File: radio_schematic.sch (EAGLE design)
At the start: 29 parts, among them J1 AUDIO_JACK_3.5MM_KIT, J2 AUDIO_JACK_3.5MM_KIT

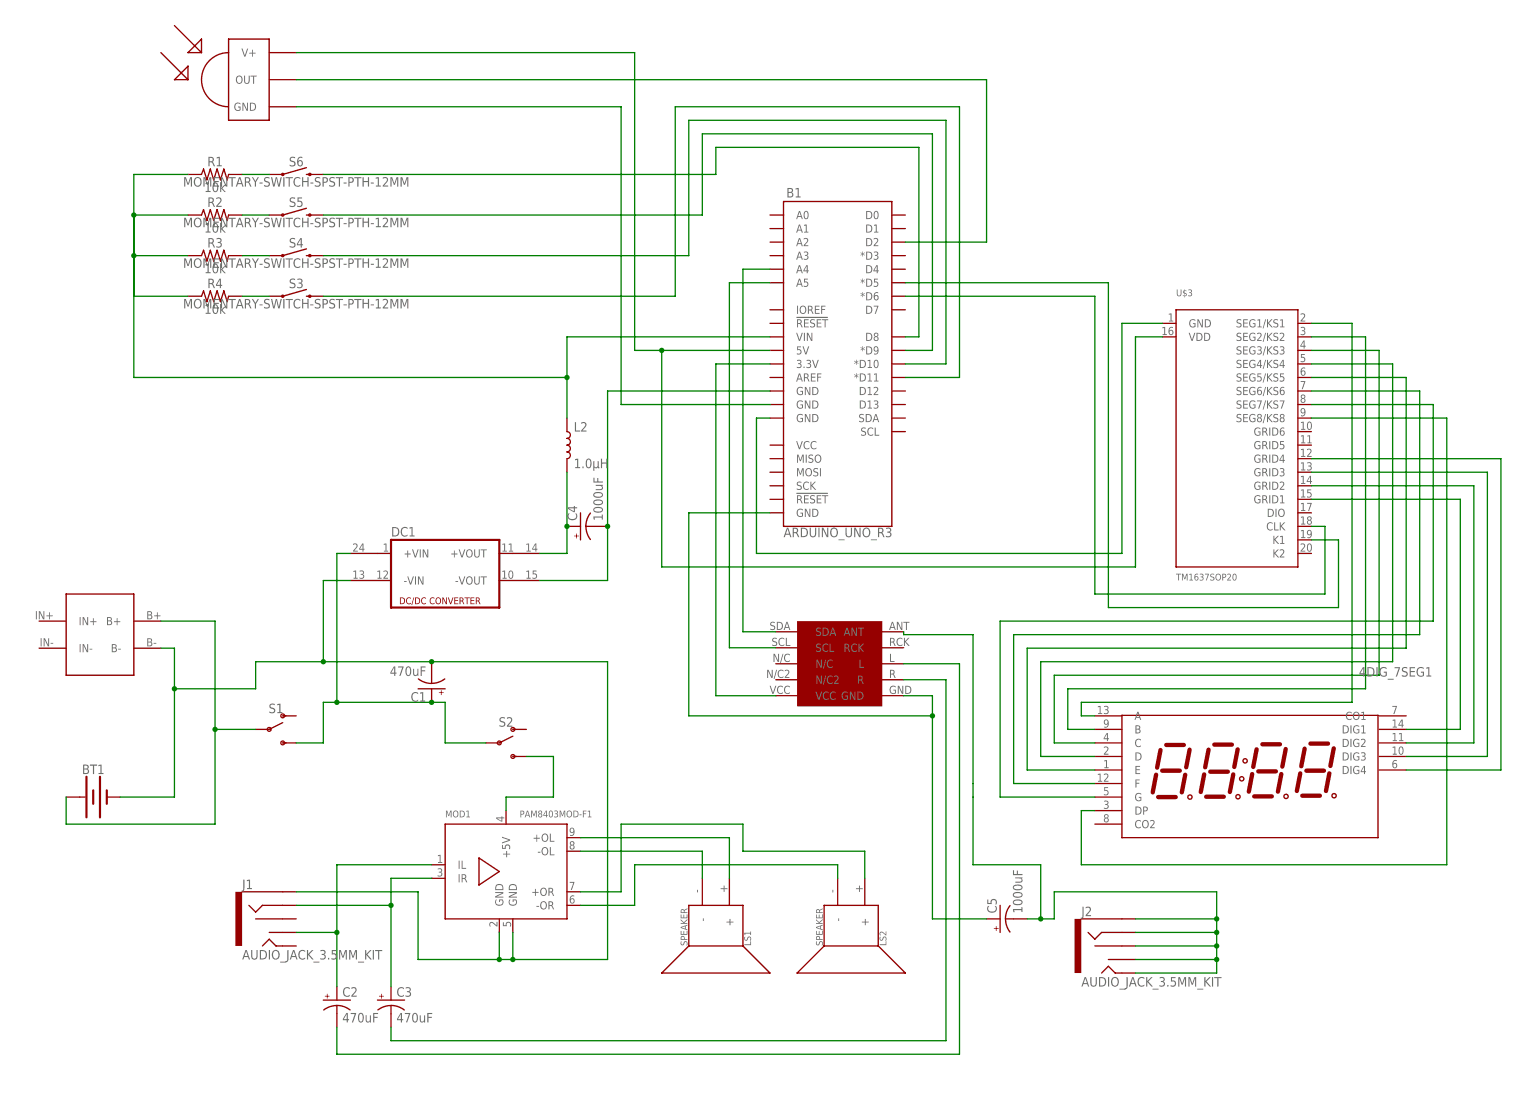
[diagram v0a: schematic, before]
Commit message: sch: add descriptions to all components and divide per section
Signed-off-by: Flopster101 <nahuelgomez329@gmail.com>
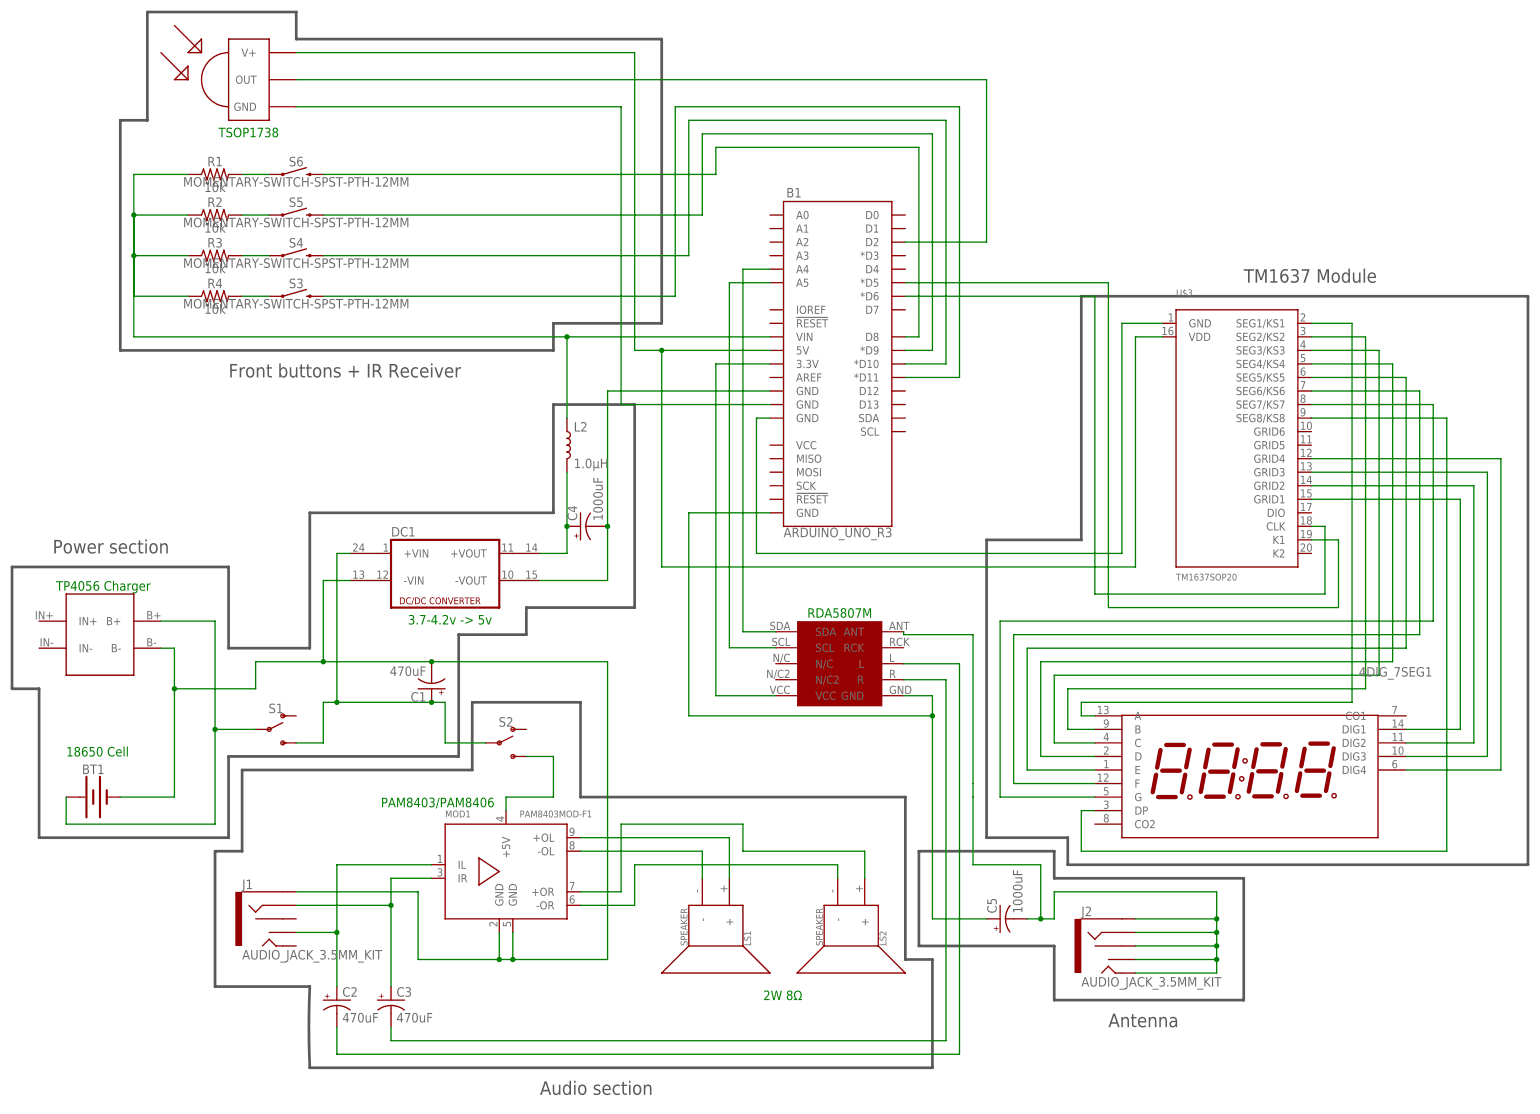
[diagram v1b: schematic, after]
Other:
- note added: "18650 Cell"
- note added: "2W 8Ω"
- note added: "3.7-4.2v -> 5v"
- note added: "Antenna"
- note added: "Audio section"
- note added: "Front buttons + IR Receiver"
- note added: "PAM8403/PAM8406"
- note added: "Power section"
- note added: "RDA5807M"
- note added: "TM1637 Module"
- note added: "TP4056 Charger"
- note added: "TSOP1738"
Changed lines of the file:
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@@
 <setting verticaltext="up"/>
 </settings>
-<grid distance="0.1" unitdist="inch" unit="inch" style="lines" multiple="1" display="no" altdistance="0.01" altunitdist="inch" altunit="inch"/>
+<grid distance="0.1" unitdist="inch" unit="inch" style="lines" multiple="1" display="yes" altdistance="0.01" altunitdist="inch" altunit="inch"/>
 <layers>
 <layer number="1" name="Top" color="4" fill="1" visible="no" active="no"/>
@@
 <sheet>
 <plain>
+<text x="98.425" y="109.855" size="1.778" layer="91">RDA5807M</text>
+<text x="23.495" y="108.585" size="1.778" layer="91">3.7-4.2v -&gt; 5v</text>
+<text x="-42.545" y="114.935" size="1.778" layer="91">TP4056 Charger</text>
+<text x="-40.64" y="83.82" size="1.778" layer="91">18650 Cell</text>
+<text x="18.415" y="74.295" size="1.778" layer="91">PAM8403/PAM8406</text>
+<text x="90.17" y="38.1" size="1.778" layer="91">2W 8Ω</text>
+<text x="-12.065" y="200.025" size="1.778" layer="91">TSOP1738</text>
+<wire x1="147.32" y1="63.5" x2="233.68" y2="63.5" width="0.508" layer="97"/>
+<wire x1="233.68" y1="63.5" x2="233.68" y2="170.18" width="0.508" layer="97"/>
+<wire x1="233.68" y1="170.18" x2="149.86" y2="170.18" width="0.508" layer="97"/>
+<wire x1="149.86" y1="170.18" x2="149.86" y2="124.46" width="0.508" layer="97"/>
+<wire x1="149.86" y1="124.46" x2="132.08" y2="124.46" width="0.508" layer="97"/>
+<wire x1="132.08" y1="124.46" x2="132.08" y2="68.58" width="0.508" layer="97"/>
+<wire x1="132.08" y1="68.58" x2="147.32" y2="68.58" width="0.508" layer="97"/>
+<wire x1="147.32" y1="68.58" x2="147.32" y2="63.5" width="0.508" layer="97"/>
+<text x="180.34" y="172.72" size="2.54" layer="97">TM1637 Module</text>
+<wire x1="144.78" y1="38.1" x2="180.34" y2="38.1" width="0.508" layer="97"/>
+<wire x1="180.34" y1="38.1" x2="180.34" y2="60.96" width="0.508" layer="97"/>
+<wire x1="180.34" y1="60.96" x2="144.78" y2="60.96" width="0.508" layer="97"/>
+<wire x1="144.78" y1="60.96" x2="144.78" y2="66.04" width="0.508" layer="97"/>
+<wire x1="144.78" y1="66.04" x2="119.38" y2="66.04" width="0.508" layer="97"/>
+<wire x1="119.38" y1="66.04" x2="119.38" y2="48.26" width="0.508" layer="97"/>
+<wire x1="119.38" y1="48.26" x2="144.78" y2="48.26" width="0.508" layer="97"/>
+<wire x1="144.78" y1="48.26" x2="144.78" y2="38.1" width="0.508" layer="97"/>
+<text x="154.94" y="33.02" size="2.54" layer="97">Antenna</text>
+<wire x1="35.56" y1="93.98" x2="35.56" y2="81.28" width="0.508" layer="97"/>
+<wire x1="35.56" y1="81.28" x2="-7.62" y2="81.28" width="0.508" layer="97"/>
+<wire x1="-7.62" y1="81.28" x2="-7.62" y2="66.04" width="0.508" layer="97"/>
+<wire x1="-7.62" y1="66.04" x2="-12.7" y2="66.04" width="0.508" layer="97"/>
+<wire x1="-12.7" y1="66.04" x2="-12.7" y2="40.64" width="0.508" layer="97"/>
+<wire x1="-12.7" y1="40.64" x2="5.08" y2="40.64" width="0.508" layer="97"/>
+<wire x1="5.08" y1="40.64" x2="5.08" y2="25.4" width="0.508" layer="97" curve="5"/>
+<wire x1="5.08" y1="25.4" x2="121.92" y2="25.4" width="0.508" layer="97"/>
+<wire x1="121.92" y1="25.4" x2="121.92" y2="45.72" width="0.508" layer="97"/>
+<wire x1="121.92" y1="45.72" x2="116.84" y2="45.72" width="0.508" layer="97"/>
+<wire x1="116.84" y1="45.72" x2="116.84" y2="76.2" width="0.508" layer="97"/>
+<wire x1="116.84" y1="76.2" x2="55.88" y2="76.2" width="0.508" layer="97"/>
+<wire x1="55.88" y1="76.2" x2="55.88" y2="93.98" width="0.508" layer="97"/>
+<wire x1="55.88" y1="93.98" x2="35.56" y2="93.98" width="0.508" layer="97"/>
+<text x="48.26" y="20.32" size="2.54" layer="97">Audio section</text>
+<wire x1="-10.16" y1="68.58" x2="-45.72" y2="68.58" width="0.508" layer="97"/>
+<wire x1="-45.72" y1="68.58" x2="-45.72" y2="96.52" width="0.508" layer="97"/>
+<wire x1="-45.72" y1="96.52" x2="-50.8" y2="96.52" width="0.508" layer="97"/>
+<wire x1="-50.8" y1="96.52" x2="-50.8" y2="119.38" width="0.508" layer="97"/>
+<wire x1="-50.8" y1="119.38" x2="-10.16" y2="119.38" width="0.508" layer="97"/>
+<wire x1="-10.16" y1="119.38" x2="-10.16" y2="104.14" width="0.508" layer="97"/>
+<wire x1="-10.16" y1="104.14" x2="5.08" y2="104.14" width="0.508" layer="97"/>
+<wire x1="5.08" y1="104.14" x2="5.08" y2="129.54" width="0.508" layer="97"/>
+<wire x1="5.08" y1="129.54" x2="50.8" y2="129.54" width="0.508" layer="97"/>
+<wire x1="50.8" y1="129.54" x2="50.8" y2="149.86" width="0.508" layer="97"/>
+<wire x1="50.8" y1="149.86" x2="66.04" y2="149.86" width="0.508" layer="97"/>
+<wire x1="66.04" y1="149.86" x2="66.04" y2="111.76" width="0.508" layer="97"/>
+<wire x1="66.04" y1="111.76" x2="45.72" y2="111.76" width="0.508" layer="97"/>
+<wire x1="45.72" y1="111.76" x2="45.72" y2="106.68" width="0.508" layer="97"/>
+<wire x1="45.72" y1="106.68" x2="33.02" y2="106.68" width="0.508" layer="97"/>
+<wire x1="33.02" y1="106.68" x2="33.02" y2="83.82" width="0.508" layer="97"/>
+<wire x1="33.02" y1="83.82" x2="-10.16" y2="83.82" width="0.508" layer="97"/>
+<wire x1="-10.16" y1="83.82" x2="-10.16" y2="68.58" width="0.508" layer="97"/>
+<text x="-43.18" y="121.92" size="2.54" layer="97">Power section</text>
+<wire x1="50.8" y1="160.02" x2="-30.48" y2="160.02" width="0.508" layer="97"/>
+<wire x1="-30.48" y1="160.02" x2="-30.48" y2="203.2" width="0.508" layer="97"/>
+<wire x1="-30.48" y1="203.2" x2="-25.4" y2="203.2" width="0.508" layer="97"/>
+<wire x1="-25.4" y1="203.2" x2="-25.4" y2="223.52" width="0.508" layer="97"/>
+<wire x1="-25.4" y1="223.52" x2="2.54" y2="223.52" width="0.508" layer="97"/>
+<wire x1="71.12" y1="218.44" x2="71.12" y2="165.1" width="0.508" layer="97"/>
+<wire x1="71.12" y1="165.1" x2="50.8" y2="165.1" width="0.508" layer="97"/>
+<wire x1="50.8" y1="165.1" x2="50.8" y2="160.02" width="0.508" layer="97"/>
+<text x="-10.16" y="154.94" size="2.54" layer="97">Front buttons + IR Receiver</text>
+<wire x1="2.54" y1="223.52" x2="2.54" y2="218.44" width="0.508" layer="97"/>
+<wire x1="2.54" y1="218.44" x2="71.12" y2="218.44" width="0.508" layer="97"/>
 </plain>
 <instances>
@@
 <wire x1="-17.78" y1="185.42" x2="-27.94" y2="185.42" width="0.1524" layer="91"/>
 <junction x="-27.94" y="185.42"/>
-<wire x1="-27.94" y1="185.42" x2="-27.94" y2="154.94" width="0.1524" layer="91"/>
+<wire x1="-27.94" y1="185.42" x2="-27.94" y2="162.56" width="0.1524" layer="91"/>
 <pinref part="B1" gate="G$1" pin="VIN"/>
-<wire x1="53.34" y1="154.94" x2="53.34" y2="162.56" width="0.1524" layer="91"/>
 <wire x1="53.34" y1="162.56" x2="91.44" y2="162.56" width="0.1524" layer="91"/>
-<wire x1="-27.94" y1="154.94" x2="53.34" y2="154.94" width="0.1524" layer="91"/>
-<junction x="53.34" y="154.94"/>
-<wire x1="53.34" y1="147.32" x2="53.34" y2="154.94" width="0.1524" layer="91"/>
+<wire x1="-27.94" y1="162.56" x2="53.34" y2="162.56" width="0.1524" layer="91"/>
+<junction x="53.34" y="162.56"/>
+<wire x1="53.34" y1="147.32" x2="53.34" y2="162.56" width="0.1524" layer="91"/>
 <pinref part="L2" gate="G$1" pin="1"/>
 </segment>
@@
 <pinref part="4DIG_7SEG1" gate="G$1" pin="DP"/>
 <wire x1="152.4" y1="73.66" x2="149.86" y2="73.66" width="0.1524" layer="91"/>
-<wire x1="149.86" y1="73.66" x2="149.86" y2="63.5" width="0.1524" layer="91"/>
-<wire x1="149.86" y1="63.5" x2="218.44" y2="63.5" width="0.1524" layer="91"/>
-<wire x1="218.44" y1="63.5" x2="218.44" y2="147.32" width="0.1524" layer="91"/>
+<wire x1="149.86" y1="73.66" x2="149.86" y2="66.04" width="0.1524" layer="91"/>
+<wire x1="149.86" y1="66.04" x2="218.44" y2="66.04" width="0.1524" layer="91"/>
+<wire x1="218.44" y1="66.04" x2="218.44" y2="147.32" width="0.1524" layer="91"/>
 <pinref part="U$3" gate="G$1" pin="SEG8/KS8"/>
 <wire x1="218.44" y1="147.32" x2="193.04" y2="147.32" width="0.1524" layer="91"/>

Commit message: sch: update schematic and add preview
Signed-off-by: Flopster101 <nahuelgomez329@gmail.com>
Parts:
- removed C1: 470uF, SparkFun-Capacitors:100UF-POLAR-RADIAL-2.5MM-25V-20%
- removed C4: 1000uF, SparkFun-Capacitors:100UF-POLAR-RADIAL-2.5MM-25V-20%
- removed DC1: (no value), dc-dc-converter:DCW1U
- removed L2: 1.0μH, SparkFun-Coils:1.0μH-0805_WIDE-1.0μH-1.4A-0.07OHM-1.4MM_H
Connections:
- removed net N$14: BT1.-, C1.-, DC1.-VIN1, J1.SLEEVE, MOD1.GND@1, MOD1.GND@2, U$4.B-
- removed net N$17: C1.+, DC1.+VIN1, S1.S, S2.P
- removed net N$40: B1.VIN, L2.1, R1.1, R2.1, R3.1, R4.1
- net N$20: now also BT1.-, J1.SLEEVE, MOD1.GND@1, MOD1.GND@2, U$4.B-; no longer C4.-, DC1.-VOUT1
- net N$43: now also B1.VIN, R1.1, R2.1, R3.1, R4.1, S1.S, S2.P; no longer C4.+, DC1.+VOUT1, L2.2
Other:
- note added: "PAM8406/LTK5208"
- note removed: "3.7-4.2v -> 5v"
- note removed: "PAM8403/PAM8406"
